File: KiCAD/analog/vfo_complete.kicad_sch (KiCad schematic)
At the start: 98 parts, among them J1 Filter Out, J10 Filter Out, J2 Filter Out, J3 Conn_01x02_Pin, J5 Conn_01x02_Pin, Q2 40673, U10 LM7171xIN, U11 LM7171xIN, U12 LM7171xIN, U13 LM7812_TO220, U14 LM317L_TO92, U21 LT1054, U22 LM7805_TO220, U5 Si5351A_Breakout

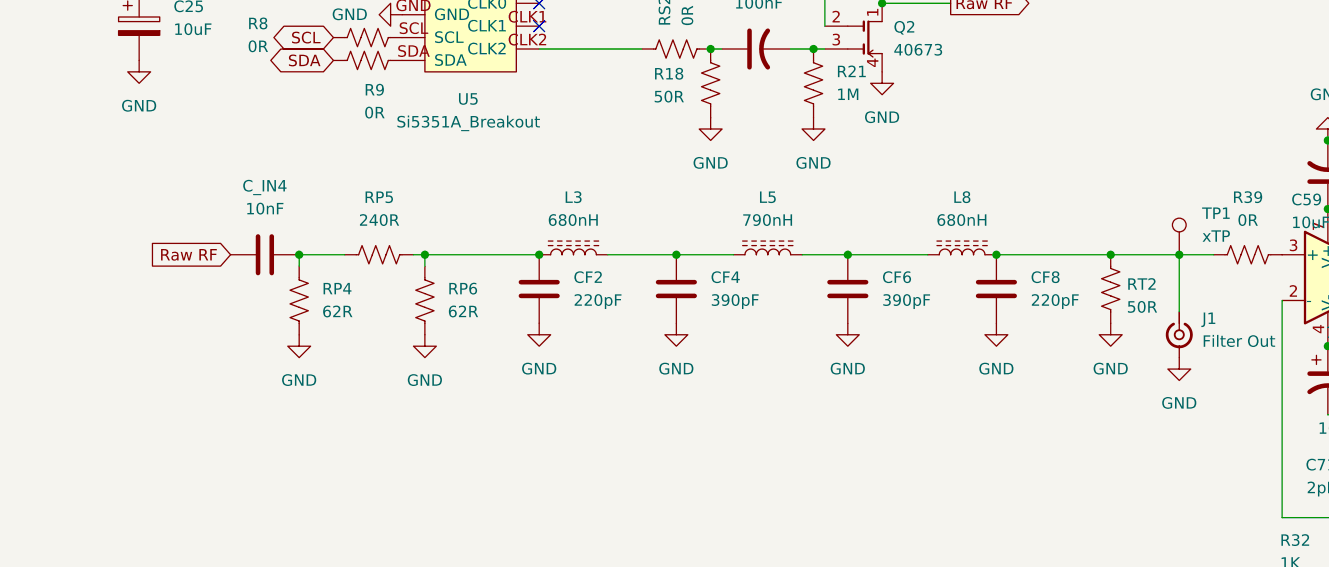
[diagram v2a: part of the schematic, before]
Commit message: KiCad revC: 4-band LPF bank populated + pad values + A_L units fix
Analog board revC: the LPF sheet is now fully populated with the
4-band relay-switched LPF bank architecture discussed in prior
sessions.  VFO sheet refactored to remove the old single-LPF stage.

LPF bank (lpf.kicad_sch):
  - 4 branches tied to a common input bus from U2 (LM7171 buffer).
    Common bus driven through C9 100nF; U2 non-inverting gain = 5.7.
  - Per-branch: 10 dB pi attenuator (100/68/100 ohm) -> 7-element
    Chebyshev CLCLCLC LPF (0.1 dB ripple, 50 ohm) -> 50 ohm RT
    terminator -> SPST relay (K1-K4) -> common output bus
    "Conditioned RF" -> R39 (0R) -> U10 input on VFO sheet.
  - Relay drive: 2N7000 low-side switcher (Q1/Q3/Q8/Q9) + 1N4148
    flyback diode (D7-D10) + screw terminal (J16/J25/J26/J27) per
    relay for coil wire termination.
  - LPF components: CF3-CF21 and L4-L17 populated with 20 m values
    (220 pF / 390 pF / 680 nH / 790 nH) on all four branches.
    Other-band values TBD per Documentation/lpf_component_values.md.
  - Pi pad resistors are now 100/68/100 (10 dB) rather than the
    initially-populated 62/240/62 (20 dB).  Reasoning: with permanent
    50 ohm termination at each LPF output and relay-based output
    switching, the pi pads are only providing impedance isolation at
    the common input bus, not inter-LPF signal isolation (which is
    handled by relay off-isolation of ~40 dB per open contact).
    10 dB is sufficient and recovers ~10 dB of noise margin.

VFO sheet (vfo_complete.kicad_sch):
  - Old inline LPF removed; VFO now feeds C10 -> U2 (on LPF sheet)
    via sheet-boundary net.
  - U10/U11/U12 LM7171 chain (post-LPF-bank amplifier + PP driver
    pair) retained.

Documentation/lpf_component_values.md (new):
  - Component values for all four bands (20/17/15/10 m).
  - 7-element Chebyshev CLCLCLC, 0.1 dB ripple, 50 ohm.
  - Per-band tables for T50-6 and T68-6 turn counts.
  - Notes on A_L unit convention (catalogs use uH/100T^2 not nH/N^2).

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
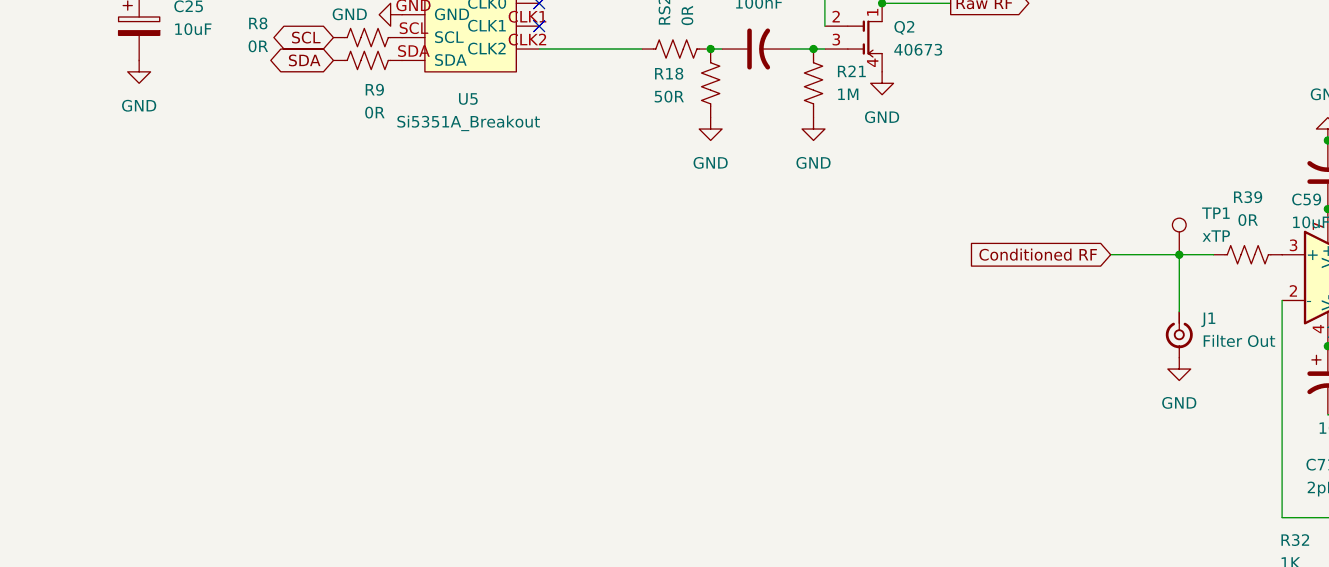
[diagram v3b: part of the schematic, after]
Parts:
- removed CF2, CF8: 220pF, Capacitor_THT:C_Disc_D6.0mm_W2.5mm_P5.00mm, symbol Device:C
- removed CF4, CF6: 390pF, Capacitor_THT:C_Disc_D7.5mm_W2.5mm_P5.00mm, symbol Device:C
- removed C_IN4: 10nF, Capacitor_THT:C_Disc_D5.0mm_W2.5mm_P5.00mm, symbol Device:C
- removed L3, L8: 680nH, xmitter:T68-6_Flat_HandWound, symbol Device:L_Ferrite
- removed L5: 790nH, xmitter:T68-6_Vertical_HandWound, symbol Device:L_Ferrite
- removed RP4, RP6: 62R, Resistor_THT:R_Axial_DIN0207_L6.3mm_D2.5mm_P10.16mm_Horizontal, symbol Device:R_US
- removed RP5: 240R, Resistor_THT:R_Axial_DIN0207_L6.3mm_D2.5mm_P10.16mm_Horizontal, symbol Device:R_US
- removed RT2: 50R, Resistor_THT:R_Axial_DIN0207_L6.3mm_D2.5mm_P10.16mm_Horizontal, symbol Device:R_US
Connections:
- net Conditioned RF: now reaches J1.1 (In), R39.1, TP1.1

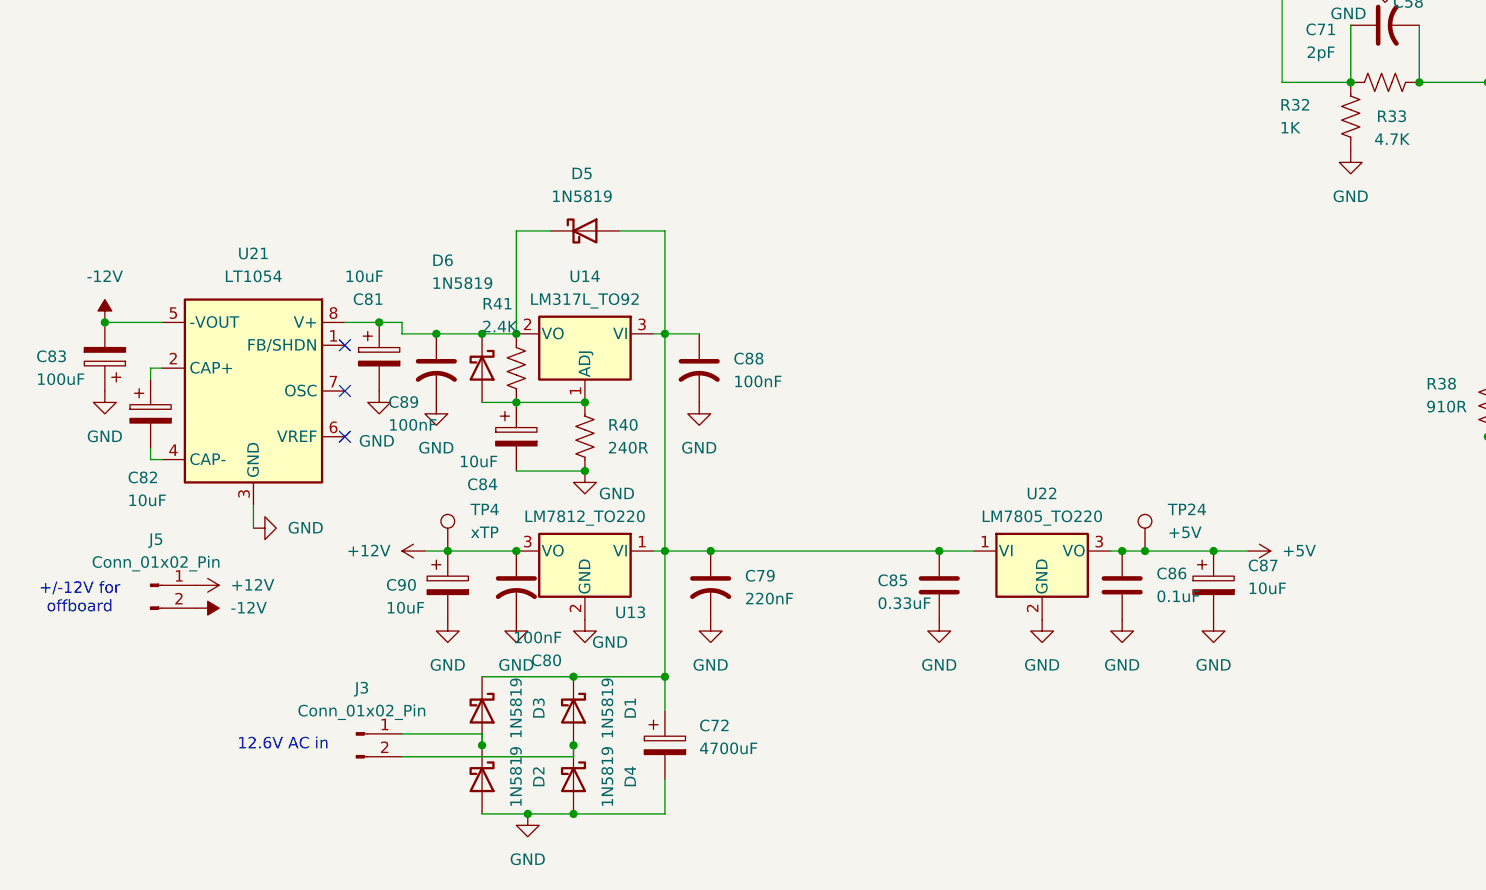
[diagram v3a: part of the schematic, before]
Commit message: KiCad revC: ±12V subsystem validated — LT1054 Fig-15 inverter + LM2940 LDO
Converged after iterating in LTspice:

* New standalone power project (KiCAD/power/) proves the topology before
  surgery on the analog project's power sheet. LT1054 as regulated inverter
  (not Figure 22 doubler — doubler was abandoned when single-FB-loop couldn't
  regulate both rails symmetrically). LM2940CT-12 LDO handles +12V from the
  13.8V bus. Both rails measure ±11.93V in sim at 1K load, VREF holds flat
  at 2.5V, V(FB_SD) settles at 0.596V.

* Datasheet-compliant divider values after discovering R16=10K violated the
  VREF ±100µA current limit: R16=20K, R17=240K (empirically tuned, differs
  from both my circuit analysis and datasheet formula — LTspice LT1054 model
  uses ~0.6V internal reference instead of the datasheet's 1.21V).
  C18=2.2nF loop comp matches datasheet "2 nF for all output voltages".

* New LM2940CT-12 symbol in xmitter.kicad_sym (TO-220-3, drop-in replacement
  for LM7812 pinout, 0.5V dropout vs 7812's 2V — needed for 13.8V-to-12V
  with headroom to spare).

* LTspice validation files in Documentation/:
    - power_sim.cir  (hand-written netlist, works in LTspice via File→Open)
    - power_sim.asc  (initial schematic attempt, retained as reference —
                      geometry is messy, use .cir instead)
    - Draft3.asc     (scratch for inspecting LT1054 symbol pin order)

Next step: migrate the validated topology into KiCAD/analog/power.kicad_sch,
replacing the shelved tube-era regulators (U15 LM317L, U19 LM7812, U23
LT1054) and the removed bridge rectifier that fed them.

Co-Authored-By: Claude Opus 4.7 <noreply@anthropic.com>
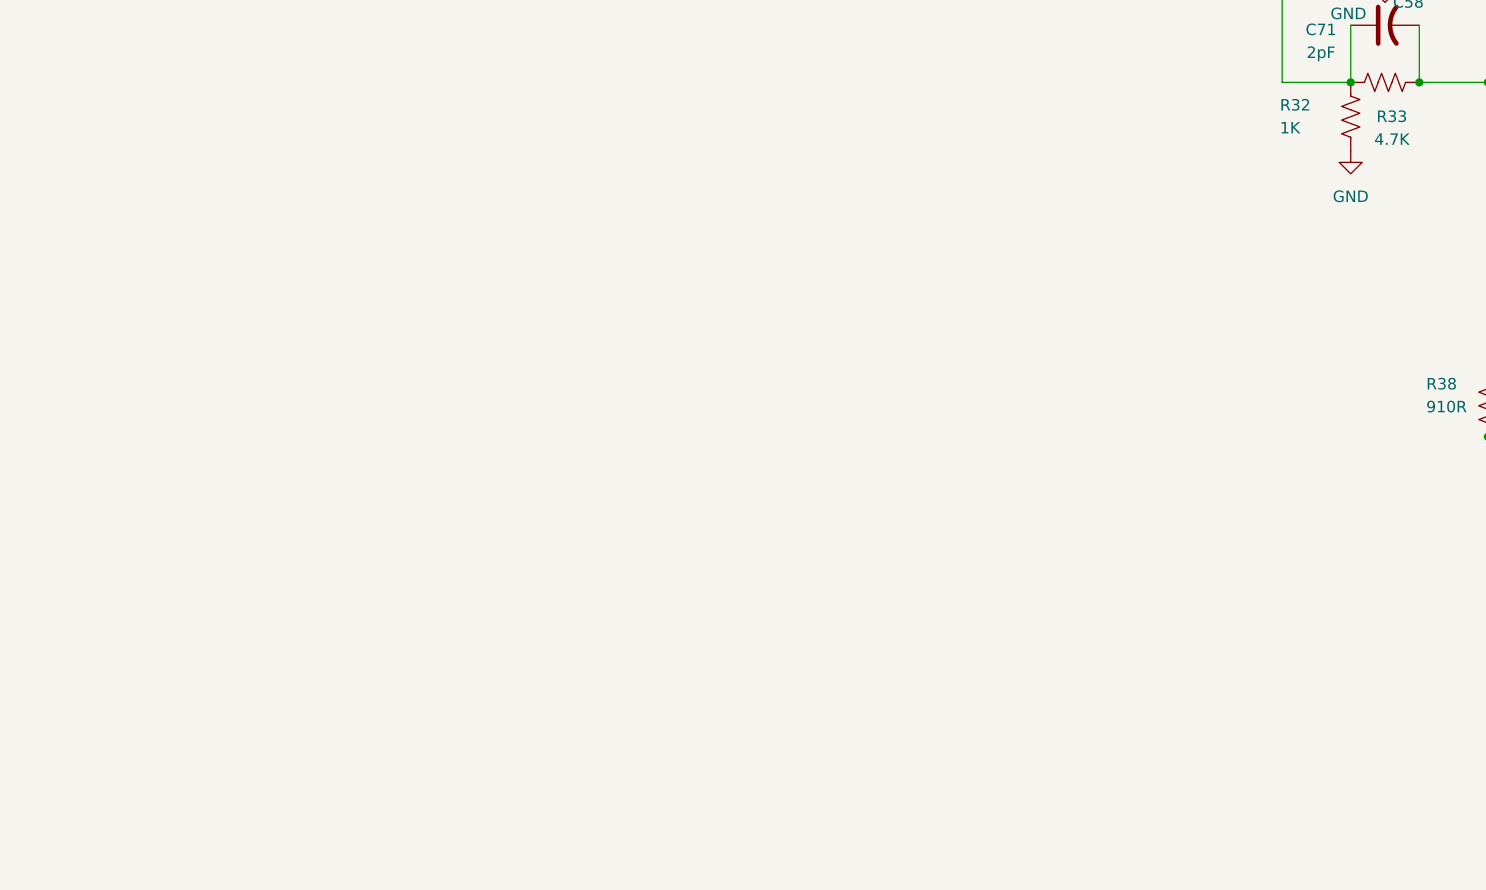
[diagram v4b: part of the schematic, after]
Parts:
- removed C72: 4700uF, xmitter:CP_Radial_Kemet_ESK_D22.0mm_P10.00mm, symbol Device:C_Polarized
- removed C79: 220nF, Capacitor_THT:C_Disc_D6.0mm_W2.5mm_P5.00mm, symbol Device:C_US
- removed C80, C88, C89: 100nF, Capacitor_THT:C_Disc_D5.0mm_W2.5mm_P5.00mm, symbol Device:C_US
- removed C81, C82, C84, C87, C90: 10uF, Capacitor_THT:CP_Radial_D5.0mm_P2.00mm, symbol Device:C_Polarized
- removed C83: 100uF, Capacitor_THT:CP_Radial_D8.0mm_P5.00mm, symbol Device:C_Polarized
- removed C85: 0.33uF, Capacitor_THT:C_Rect_L7.0mm_W3.5mm_P5.00mm, symbol Device:C
- removed C86: 0.1uF, Capacitor_THT:C_Disc_D5.0mm_W2.5mm_P5.00mm, symbol Device:C
- removed D1, D2, D3, D4, D5, D6: 1N5819, Diode_THT:D_DO-41_SOD81_P10.16mm_Horizontal, symbol Diode:1N5819
- removed J3, J5: Conn_01x02_Pin, TerminalBlock_Phoenix:TerminalBlock_Phoenix_MKDS-1,5-2_1x02_P5.00mm_Horizontal, symbol Connector:Conn_01x02_Pin
- removed R40: 240R, Resistor_THT:R_Axial_DIN0207_L6.3mm_D2.5mm_P10.16mm_Horizontal, symbol Device:R_US
- removed R41: 2.4K, Resistor_THT:R_Axial_DIN0207_L6.3mm_D2.5mm_P10.16mm_Horizontal, symbol Device:R_US
- removed TP24: +5V, Connector_PinHeader_2.54mm:PinHeader_1x01_P2.54mm_Vertical, symbol xmitter:xTP
- removed TP4: xTP, Connector_PinHeader_2.54mm:PinHeader_1x01_P2.54mm_Vertical, symbol xmitter:xTP
- removed U13: LM7812_TO220, Package_TO_SOT_THT:TO-220-3_Vertical, symbol Regulator_Linear:LM7812_TO220
- removed U14: LM317L_TO92, Package_TO_SOT_THT:TO-92_Inline_Wide, symbol Regulator_Linear:LM317L_TO92
- removed U21: LT1054, Package_DIP:DIP-8_W7.62mm, symbol Regulator_SwitchedCapacitor:LT1054
- removed U22: LM7805_TO220, Package_TO_SOT_THT:TO-220-3_Vertical, symbol Regulator_Linear:LM7805_TO220
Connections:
- no-connect marks 5 -> 2
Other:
- note removed: "+/-12V for offboard"
- note removed: "12.6V AC in"

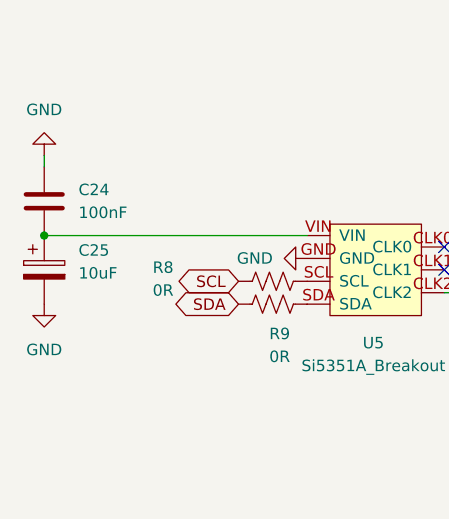
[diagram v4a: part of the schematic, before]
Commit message: KiCad revC: +28V doubler + 5V LDO added to analog/power, ERC clean
- Migrated LT1054 Figure 20 positive doubler from standalone power project
  into analog/power.kicad_sch for the +28V reed-relay rail
- Added LM2940CT-5.0 LDO stage for Metro / Si5351 +5V rail
- analog ERC: 4 messages, all classified as false positives (U9 pin 5
  tied to GND per Fig 20 topology, PCF_P5_SPARE intentionally unused,
  VIN pins now driven by added +5V rail)
- Added QRP Labs 10W PA / 5W PA reference PDFs + 2N7000 + lm2940c
  datasheets to Documentation/QRP_Examples/

Co-Authored-By: Claude Opus 4.7 <noreply@anthropic.com>
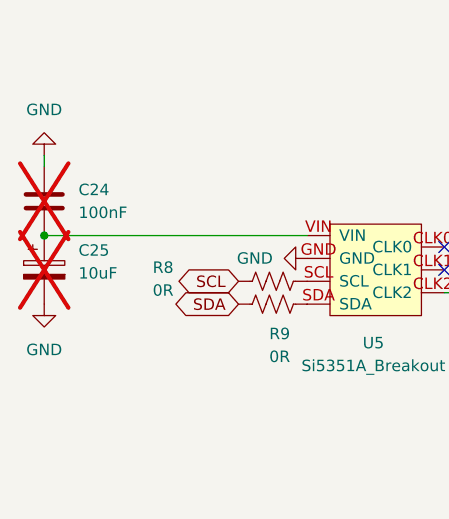
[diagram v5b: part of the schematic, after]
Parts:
- C24, C25: now not fitted
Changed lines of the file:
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@@
 		(on_board yes)
 		(in_pos_files yes)
-		(dnp no)
+		(dnp yes)
 		(fields_autoplaced yes)
 		(property "Reference" "C25"
@@
 		(on_board yes)
 		(in_pos_files yes)
-		(dnp no)
+		(dnp yes)
 		(fields_autoplaced yes)
 		(property "Reference" "C24"
